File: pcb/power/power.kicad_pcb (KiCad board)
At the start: 2 copper layers, 96 parts, among them CON1 BARREL_JACK, P1 CONN_01X04, P2 CONN_01X04, P3 CONN_01X04, P4 CONN_01X03, P5 USB_A, P6 CONN_01X03, Q1 MMBT3904, Q2 MMBT3904, Q3 MMBT3904, Q4 MMBT3904, Q5 MMBT3904, Q6 MMBT3904, Q7 DMG2305UX, Q8 DMG2305UX, Q9 DMG2305UX, U1 LM2840, U2 TS30012, U3 LM324QT

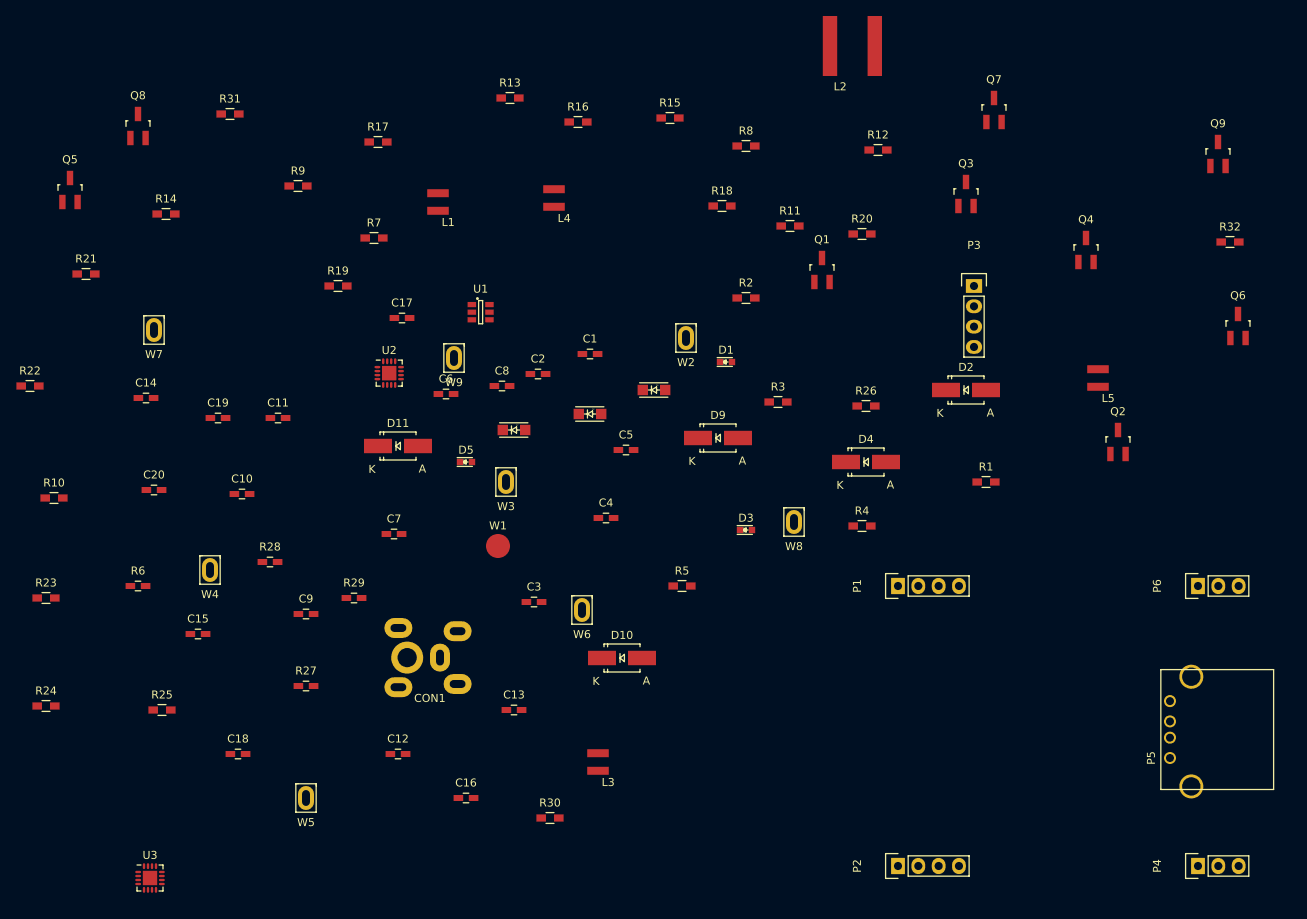
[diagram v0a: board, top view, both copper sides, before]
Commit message: Started placing some components.
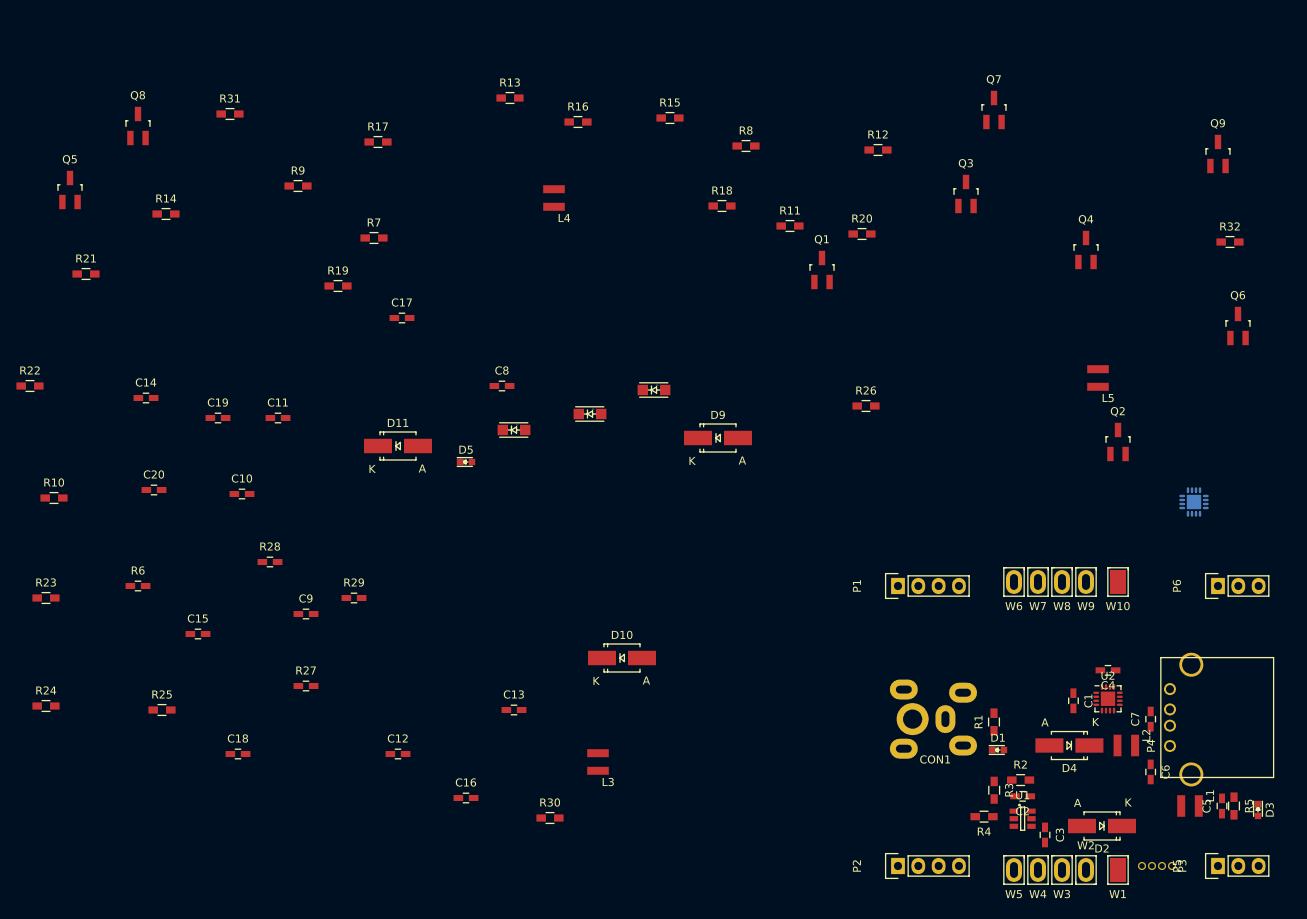
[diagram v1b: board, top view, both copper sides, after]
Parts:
- added W10: TEST_1P, Additional:GND_PROBE, F.Cu at (160.0, 87.0)
- L2: value 4.7u -> 33u; footprint Additional:Taiyo_Yuden_NRS8030_IND -> Additional:Bourns_SRN3015
- P3: footprint Pin_Headers:Pin_Header_Straight_1x04 -> Additional:LED_CONN_1.25_PITCH
- P4: value CONN_01X03 -> USB_A; footprint Pin_Headers:Pin_Header_Straight_1x03 -> Connect:USB_A
- P5: value USB_A -> CONN_01X03; footprint Connect:USB_A -> Pin_Headers:Pin_Header_Straight_1x03
- U3: moved to B.Cu
- W1: footprint Measurement_Points:Measurement_Point_Round-SMD-Pad_Big -> Additional:GND_PROBE
- moved U3 138.7 mm to (169.5, 77.0)
- moved L1 120.6 mm to (169.0, 115.0), turned to 90 degrees
- moved W7 114.9 mm to (150.0, 87.0)
- moved W4 110.1 mm to (150.0, 123.0)
- moved C6 100.0 mm to (164.1, 110.7), turned to 270 degrees
- moved U2 98.6 mm to (158.8, 101.6)
- moved C7 97.4 mm to (164.1, 104.1), turned to 90 degrees
- moved L2 95.0 mm to (161.0, 107.4), turned to 90 degrees
- moved U1 92.7 mm to (148.1, 116.6)
- moved W5 89.0 mm to (147.0, 123.0)
- moved W1 87.4 mm to (160.0, 123.0)
- moved C5 86.8 mm to (173.0, 115.0), turned to 90 degrees
- moved W3 84.7 mm to (153.0, 123.0)
- moved W9 83.8 mm to (156.0, 87.0)
- moved W2 83.2 mm to (156.0, 123.0), turned to 180 degrees
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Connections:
- P4 pad 1: GND -> V5
- P4 pad 2: 5V_EN -> (no net)
- P4 pad 3: V28 -> (no net)
- P5 pad 1: V5 -> GND
- P5 pad 2: Net-(P5-Pad2) -> 5V_EN
- P5 pad 3: Net-(P5-Pad3) -> V28

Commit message: Finished both bucket converters.
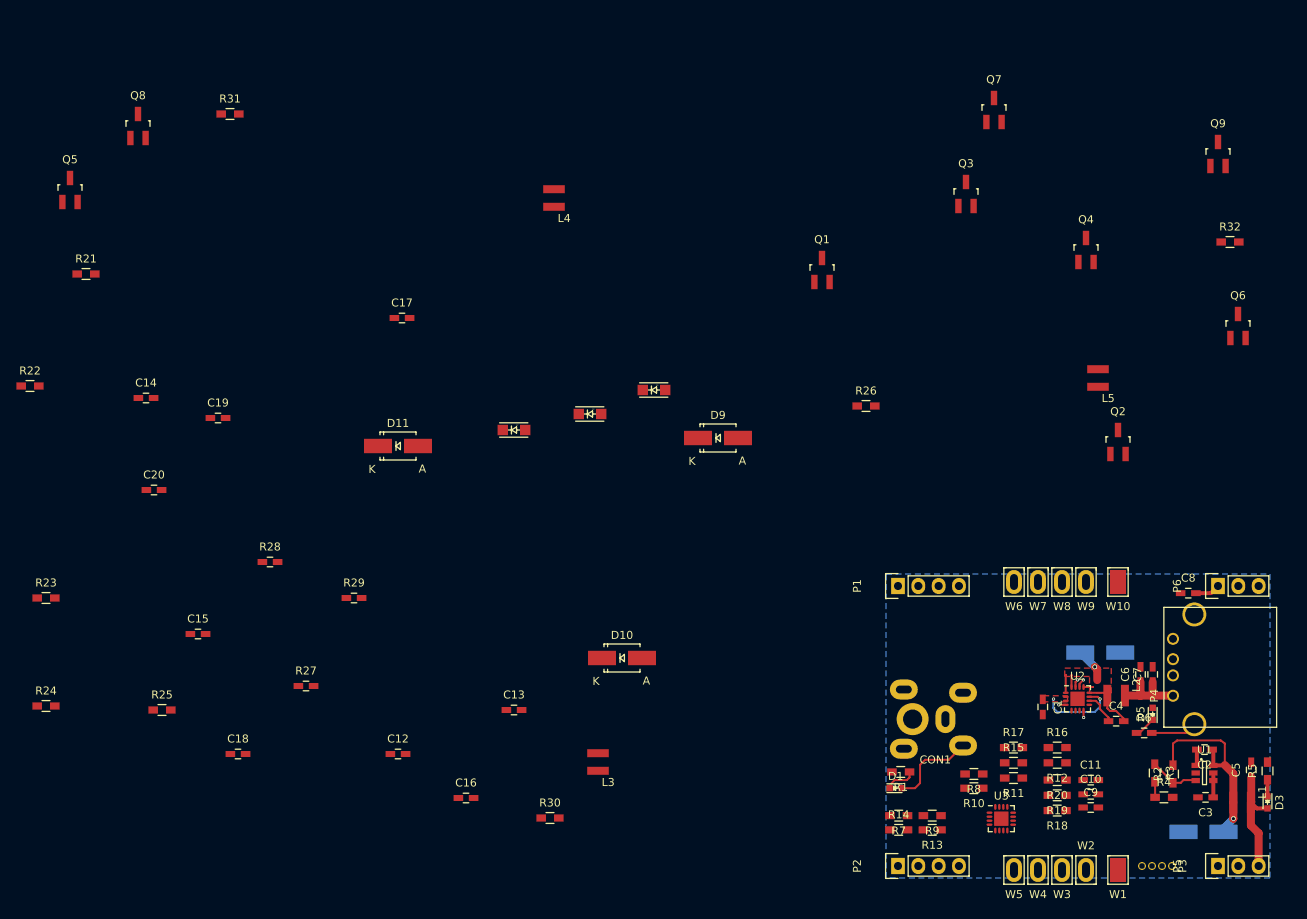
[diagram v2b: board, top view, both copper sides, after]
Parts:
- D2, D4: moved to B.Cu
- U3: moved to F.Cu
- moved R6 127.1 mm to (163.3, 105.9)
- moved R10 120.6 mm to (142.0, 112.8), turned to 180 degrees
- moved R14 119.6 mm to (132.6, 118.0)
- moved C10 112.5 mm to (156.6, 113.5)
- moved R9 111.7 mm to (136.8, 116.2), turned to 180 degrees
- moved C11 111.2 mm to (156.6, 111.8)
- moved R19 110.2 mm to (152.4, 113.7), turned to 180 degrees
- moved R17 109.7 mm to (146.9, 107.7)
- moved R13 105.6 mm to (136.8, 118.0), turned to 180 degrees
- moved C9 101.0 mm to (156.6, 115.2)
- moved R16 98.5 mm to (152.4, 107.7)
- moved R7 97.5 mm to (132.6, 116.2), turned to 180 degrees
- moved D5 91.4 mm to (164.3, 103.5), turned to 90 degrees
- moved R15 91.3 mm to (146.9, 109.6)
- moved C8 89.6 mm to (168.8, 88.4)
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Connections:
- C6 pad 2: Net-(C6-Pad2) -> GND
- C7 pad 2: Net-(C6-Pad2) -> GND
- D4 pad 2: Net-(C6-Pad2) -> GND
- R6 pad 2: Net-(C6-Pad2) -> GND
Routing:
- net Net-(C2-Pad1): track 0.00 -> 25.9 mm, vias 0 -> 1
- net V20: track 0.00 -> 24.7 mm, vias 0 -> 2
- net Net-(C4-Pad2): track 0.00 -> 16.1 mm, vias 0 -> 1
- net V28: track 0.00 -> 13.9 mm
- net GND: track 0.00 -> 9.61 mm, vias 0 -> 4
- net V5: track 0.00 -> 9.50 mm
- net Net-(R2-Pad1): track 0.00 -> 6.67 mm
- net Net-(C4-Pad1): track 0.00 -> 4.01 mm
- net Net-(D1-Pad1): track 0.00 -> 3.95 mm
- net VOLED: track 0.00 -> 3.14 mm
- net Net-(D5-Pad1): track 0.00 -> 2.70 mm
- net Net-(D3-Pad1): track 0.00 -> 2.29 mm
- net Net-(C2-Pad2): track 0.00 -> 2.03 mm
- net Net-(R3-Pad2): track 0.00 -> 1.97 mm
- added copper zone on B.Cu, net GND
- added copper zone on F.Cu, net Net-(C4-Pad2)
- added copper zone on F.Cu, net V20
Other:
- rule via_min_drill: 0.3 -> 0.2

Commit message: Did a lot of stuff. Currently working on the exact 3D models for the headers.
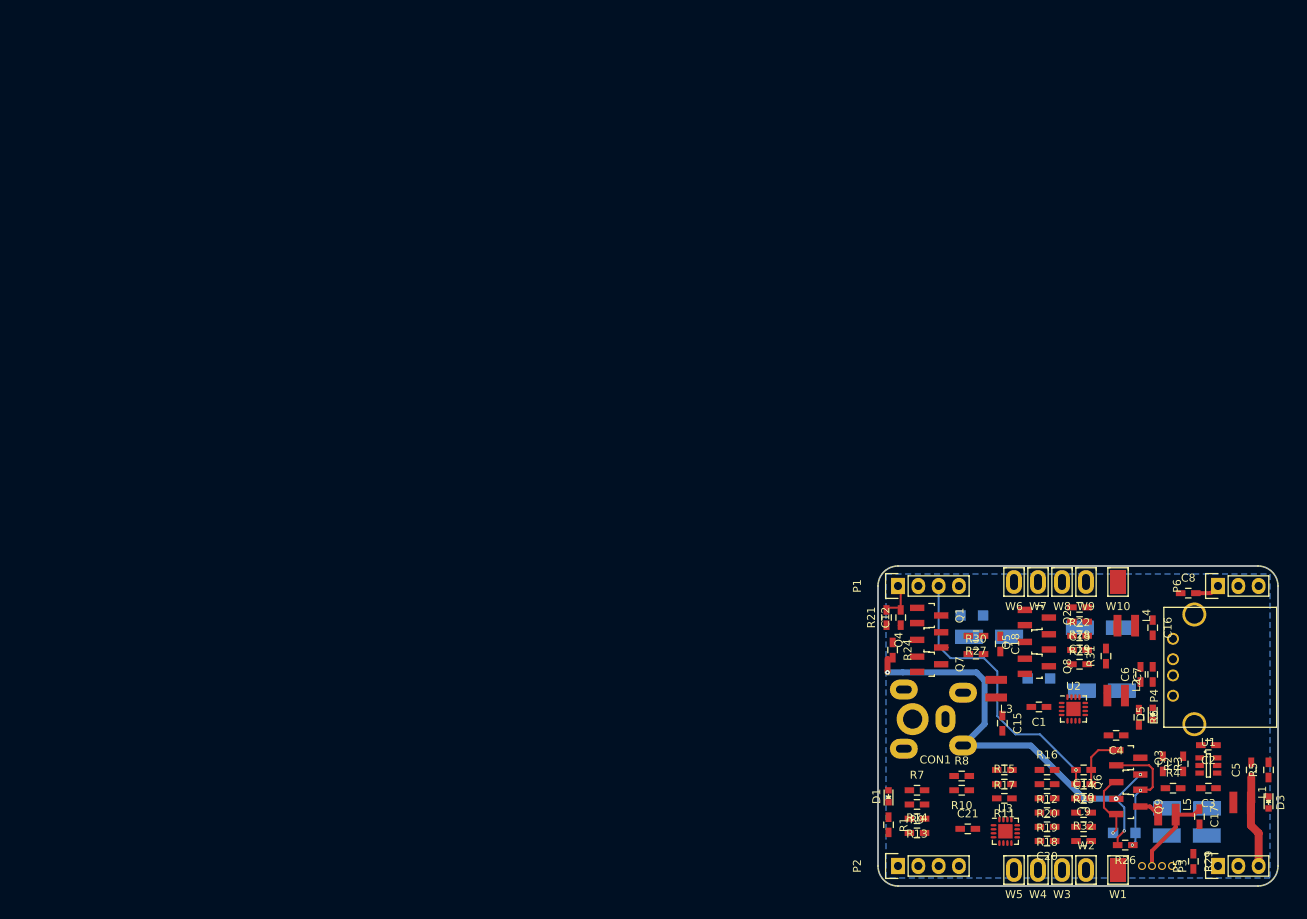
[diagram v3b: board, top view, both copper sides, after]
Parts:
- added C21: 2.2u, Capacitors_SMD:C_0603_HandSoldering, F.Cu at (141.2, 117.9)
- D10, D11, D6, D7, D8, D9: moved to B.Cu
- R1, R10, R11, R12, R13, R14, R15, R16, R17, R18, R19, R2, R20, R21, R22, R23, R24, R25, R26, R3, R30, R31, R32, R4, R5, R7, R8, R9: footprint Resistors_SMD:R_0603_HandSoldering -> Additional:R_0603_HandSoldering_Same_As_C
- R27, R28, R29, R6: footprint Capacitors_SMD:C_0603_HandSoldering -> Additional:R_0603_HandSoldering_Same_As_C
- moved R22 134.1 mm to (155.2, 90.2), turned to 180 degrees
- moved Q5 133.4 mm to (149.9, 94.5), turned to 90 degrees
- moved R23 131.8 mm to (155.7, 112.3), turned to 180 degrees
- moved Q8 131.1 mm to (149.9, 97.5), turned to 270 degrees
- moved R31 128.8 mm to (158.5, 96.3), turned to 90 degrees
- moved C14 126.1 mm to (155.7, 110.5), turned to 180 degrees
- moved C20 119.9 mm to (151.1, 119.4), turned to 180 degrees
- moved C17 117.6 mm to (170.2, 116.3), turned to 270 degrees
- moved R25 115.1 mm to (155.2, 93.7), turned to 180 degrees
- moved C19 112.0 mm to (155.2, 97.3)
- moved R29 110.0 mm to (169.4, 121.9), turned to 270 degrees
- moved R21 108.9 mm to (131.1, 91.4), turned to 90 degrees
- moved D11 108.5 mm to (168.6, 115.3)
- moved R24 106.1 mm to (131.8, 95.5), turned to 270 degrees
- moved R28 101.8 mm to (155.2, 95.5)
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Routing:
- net PWM_G: track 0.00 -> 36.2 mm, vias 0 -> 1
- net V20: track 24.7 -> 58.2 mm, vias 2 -> 4
- net Net-(C2-Pad1): track 25.9 -> 0.00 mm, vias 1 -> 0
- net Net-(D8-Pad1): track 0.00 -> 16.1 mm, vias 0 -> 2
- net Net-(C4-Pad2): track 16.1 -> 0.49 mm, vias 1 -> 0
- net LED_G: track 0.00 -> 10.9 mm
- net GND: track 9.61 -> 0.00 mm, vias 4 -> 0
- net V5: track 9.50 -> 0.02 mm
- net Net-(D8-Pad2): track 0.00 -> 8.46 mm, vias 0 -> 1
- net Net-(C14-Pad1): track 0.00 -> 6.87 mm
- net Net-(R2-Pad1): track 6.67 -> 0.00 mm
- net PWM_R: track 0.00 -> 4.54 mm
- net Net-(C4-Pad1): track 4.01 -> 0.00 mm
- net Net-(D1-Pad1): track 3.95 -> 0.00 mm
- net Net-(D5-Pad1): track 2.70 -> 0.00 mm
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- removed copper zone on F.Cu, net Net-(C4-Pad2)
- removed copper zone on F.Cu, net V20
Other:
- board outline added: 50 x 40 mm

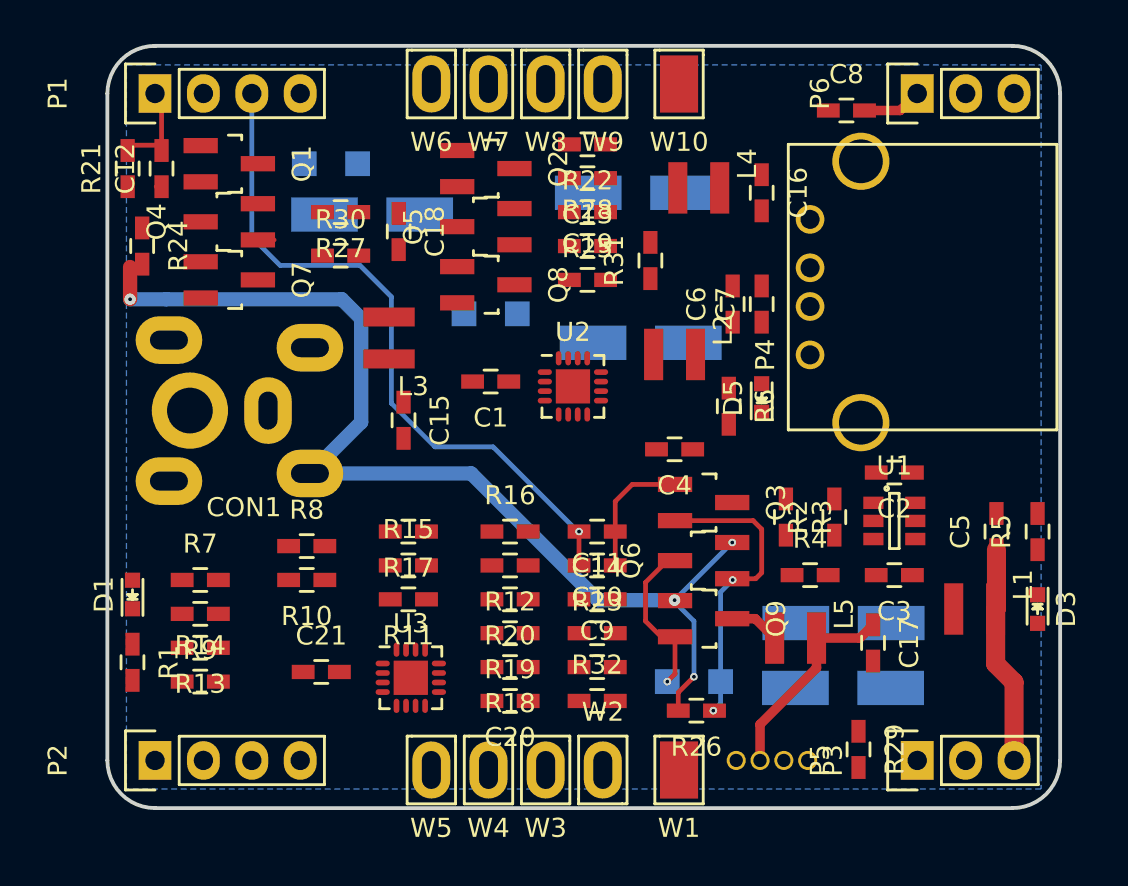
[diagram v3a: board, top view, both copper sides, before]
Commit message: Almost finished routing.
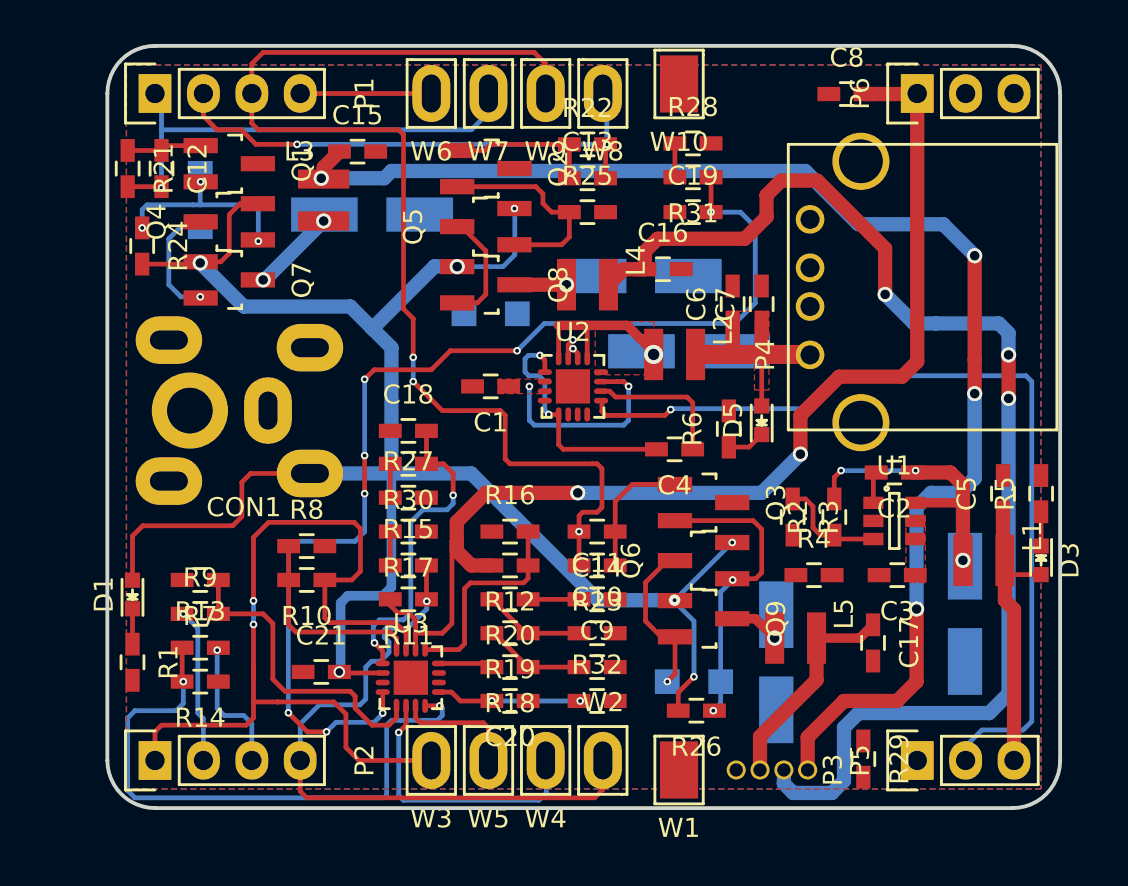
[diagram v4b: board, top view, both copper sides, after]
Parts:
- P1, P2: footprint Pin_Headers:Pin_Header_Straight_1x04 -> Additional:ESQ-104-12-G-S-LL
- P5, P6: footprint Pin_Headers:Pin_Header_Straight_1x03 -> Additional:ESQ-103-12-G-S-LL
- moved R27 15.4 mm to (145.8, 108.7), turned to 0 degrees
- moved C15 14.3 mm to (143.1, 90.6), turned to 0 degrees
- moved R30 11.5 mm to (145.8, 106.9), turned to 180 degrees
- moved C18 10.5 mm to (145.8, 105.2), turned to 0 degrees
- moved L3 8.01 mm to (141.4, 93.1), turned to 180 degrees
- moved L4 7.74 mm to (155.2, 97.5)
- moved R28 7.72 mm to (160.7, 90.1)
- moved D2 7.49 mm to (175.0, 114.8), turned to 270 degrees
- moved D6 7.12 mm to (134.9, 93.1), turned to 90 degrees
- moved C19 6.58 mm to (160.7, 93.7)
- moved C16 6.55 mm to (159.2, 96.7), turned to 0 degrees
- moved W3 6.02 mm to (147.0, 122.5)
- moved R31 4.91 mm to (160.7, 91.9), turned to 180 degrees
- moved D10 4.38 mm to (158.0, 97.1)
- moved D11 4.09 mm to (165.1, 117.3), turned to 270 degrees
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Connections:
- P4 pad 2: (no net) -> Net-(P4-Pad2)
- P4 pad 3: (no net) -> Net-(P4-Pad3)
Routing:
- net LED_R: track 0.00 -> 71.4 mm, vias 0 -> 4
- net LED_B: track 0.00 -> 64.6 mm, vias 0 -> 3
- net /LEDs/LED Driver 3 Chan. /OPAMP_B: track 0.00 -> 58.6 mm, vias 0 -> 8
- net VOLED: track 3.14 -> 59.6 mm, vias 0 -> 2
- net V20: track 58.2 -> 112.8 mm, vias 4 -> 9
- net 5V_EN: track 0.00 -> 46.9 mm, vias 0 -> 1
- net ADC_R: track 0.00 -> 46.6 mm, vias 0 -> 2
- net ADC_OLED: track 0.00 -> 34.8 mm, vias 0 -> 1
- net Net-(R13-Pad1): track 0.00 -> 32.0 mm, vias 0 -> 2
- net PWM_B: track 0.00 -> 27.6 mm, vias 0 -> 2
- net PWM_G: track 36.2 -> 62.6 mm, vias 1 -> 3
- net Net-(C4-Pad2): track 0.49 -> 23.5 mm, vias 0 -> 3
- net ADC_B: track 0.00 -> 22.8 mm, vias 0 -> 2
- net PWM_R: track 4.54 -> 27.1 mm, vias 0 -> 1
- net /LEDs/LED Driver 3 Chan. /OPAMP_R: track 0.00 -> 16.7 mm, vias 0 -> 2
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- added copper zone on F.Cu, net GND
- added copper zone on F.Cu, net Net-(C4-Pad2)
- added copper zone on F.Cu, net V20
- added copper zone on F.Cu, net V5

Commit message: Finished layout.
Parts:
- moved C1 0.86 mm to (149.3, 102.9)
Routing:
- net PWM_OLED: track 9.55 -> 81.6 mm, vias 0 -> 3
- net LED_GND: track 3.56 -> 74.5 mm, vias 0 -> 4
- net V20: track 112.8 -> 157.4 mm, vias 9 -> 15
- net ADC_B: track 22.8 -> 62.9 mm
- net ADC_G: track 13.7 -> 30.1 mm, vias 1 -> 3
- net Net-(U3-Pad10): track 0.00 -> 8.74 mm, vias 0 -> 2
- net GND: track 1.68 -> 8.54 mm, vias 2 -> 6
- net Net-(D7-Pad1): track 11.4 -> 16.9 mm, vias 0 -> 1
- net Net-(C4-Pad2): track 23.5 -> 28.5 mm
- net Net-(R3-Pad2): track 0.00 -> 2.17 mm
- net VOLED: track 59.6 -> 61.3 mm
- net PWM_G: track 62.6 -> 61.6 mm
- net Net-(R13-Pad1): track 32.0 -> 31.0 mm
- net LED_R: track 71.4 -> 70.5 mm
- net ADC_OLED: track 34.8 -> 34.0 mm
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- removed copper zone on F.Cu, net Net-(C4-Pad2)
- removed copper zone on F.Cu, net V20
- removed copper zone on F.Cu, net V5
